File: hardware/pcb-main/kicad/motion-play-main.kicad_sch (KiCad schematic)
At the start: 24 parts, among them J3 LED_Strip, J4 Conn_01x05, J5 Conn_01x05, J6 Conn_01x05, U1 AP2112K-3.3TRG1, U2 T-Display-S3

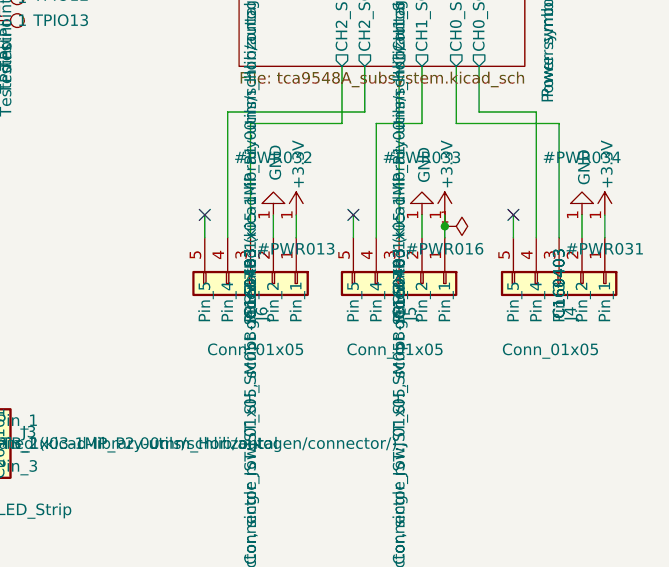
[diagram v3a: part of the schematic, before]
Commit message: JLCPCB pre-flight review: fix 3 LCSC part numbers, add fabrication files
Pre-flight review for JLCPCB fabrication + SMT assembly submission.

LCSC part fixes (data-only, no schematic/PCB design changes):
- J4/J5/J6: C160403 (3-pin JST-SH) → C136657 (5-pin SM05B-SRSS-TB)
- R27: C500724 (0.1Ω 2W, out of stock) → C2903476 (0.1Ω 3W, 94k stock)
- Q2: C3040193 (VBZ3401, 3 units) → C15127 (AO3401A, 1.45M stock, Basic)

Adds fabrication exports (Fabrication Toolkit plugin):
- BOM, CPL/positions, designators, netlist
- DRC and ERC reports
- Pre-flight review report (preflight-review.md)

Remaining advisory: BQ24195RGER (C90862) has only 22 units — order soon.

Made-with: Cursor
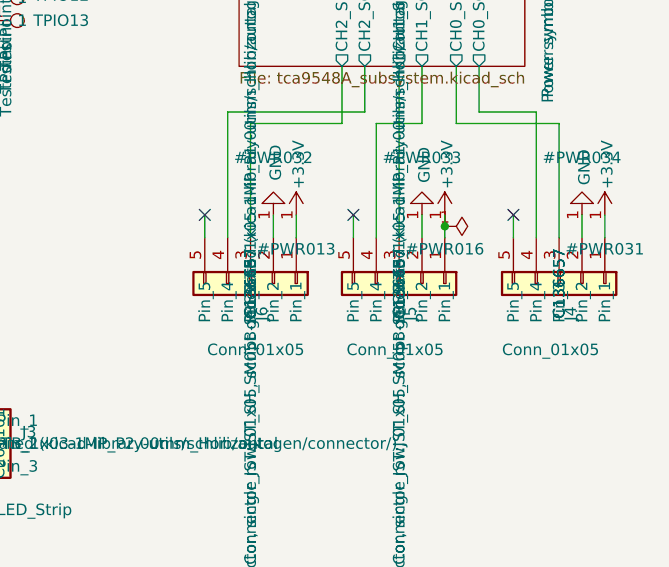
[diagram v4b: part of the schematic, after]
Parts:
- J4, J5, J6: LCSC Part C160403 -> C136657; LCSC Part No C160403 -> C136657
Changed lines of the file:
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@@
 			)
 		)
-		(property "LCSC Part No" "C160403"
+		(property "LCSC Part No" "C136657"
 			(at 205.74 135.89 0)
 			(effects
@@
 			)
 		)
-		(property "LCSC Part" "C160403"
+		(property "LCSC Part" "C136657"
 			(at 205.74 135.89 0)
 			(effects
@@
 			)
 		)
-		(property "LCSC Part No" "C160403"
+		(property "LCSC Part No" "C136657"
 			(at 187.96 135.89 0)
 			(effects
@@
 			)
 		)
-		(property "LCSC Part" "C160403"
+		(property "LCSC Part" "C136657"
 			(at 187.96 135.89 0)
 			(effects
@@
 			)
 		)
-		(property "LCSC Part No" "C160403"
+		(property "LCSC Part No" "C136657"
 			(at 171.45 135.89 0)
 			(effects
@@
 			)
 		)
-		(property "LCSC Part" "C160403"
+		(property "LCSC Part" "C136657"
 			(at 171.45 135.89 0)
 			(effects

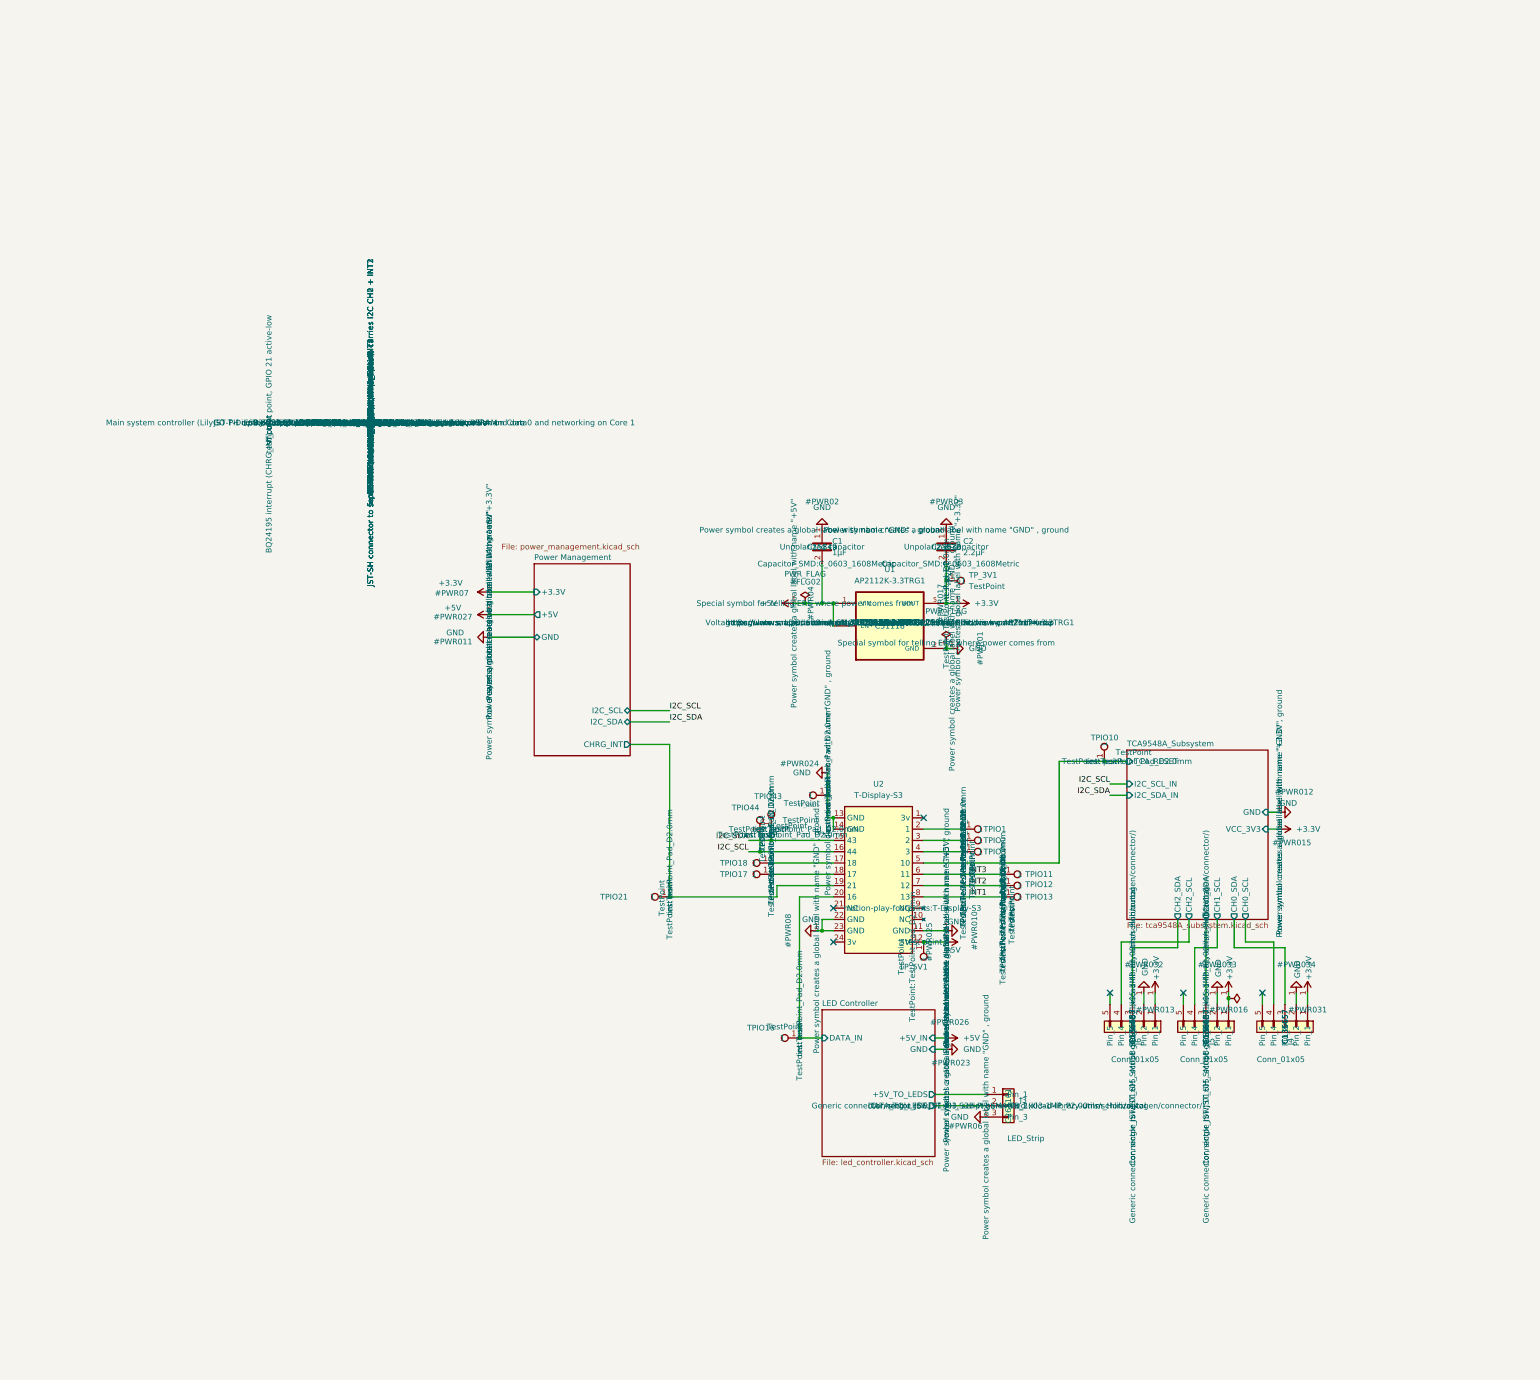
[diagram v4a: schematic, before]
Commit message: Generate ESP32-S3 schematic sheet and apply integration modifications
Phase 1c: created esp32_spec.json and generate_esp32_sheet.py to produce
esp32_s3.kicad_sch with WROOM-1 module, EN/boot circuits, USB series
resistors, decoupling caps, and status LED. All components annotated via
centralized annotate.py.

Phase 1d partial: esp32_integration.py placed AMS1117, USBLC6, power
switch, USB hierarchical labels on power_management sheet; added ESP32
sheet reference and removed U2/U1/unused test points from root sheet.

Fixed modify.py annotate.py path resolution bug. Fixed generator UUID
mismatch that caused kiutils to reset reference designators to '?'.

Made-with: Cursor
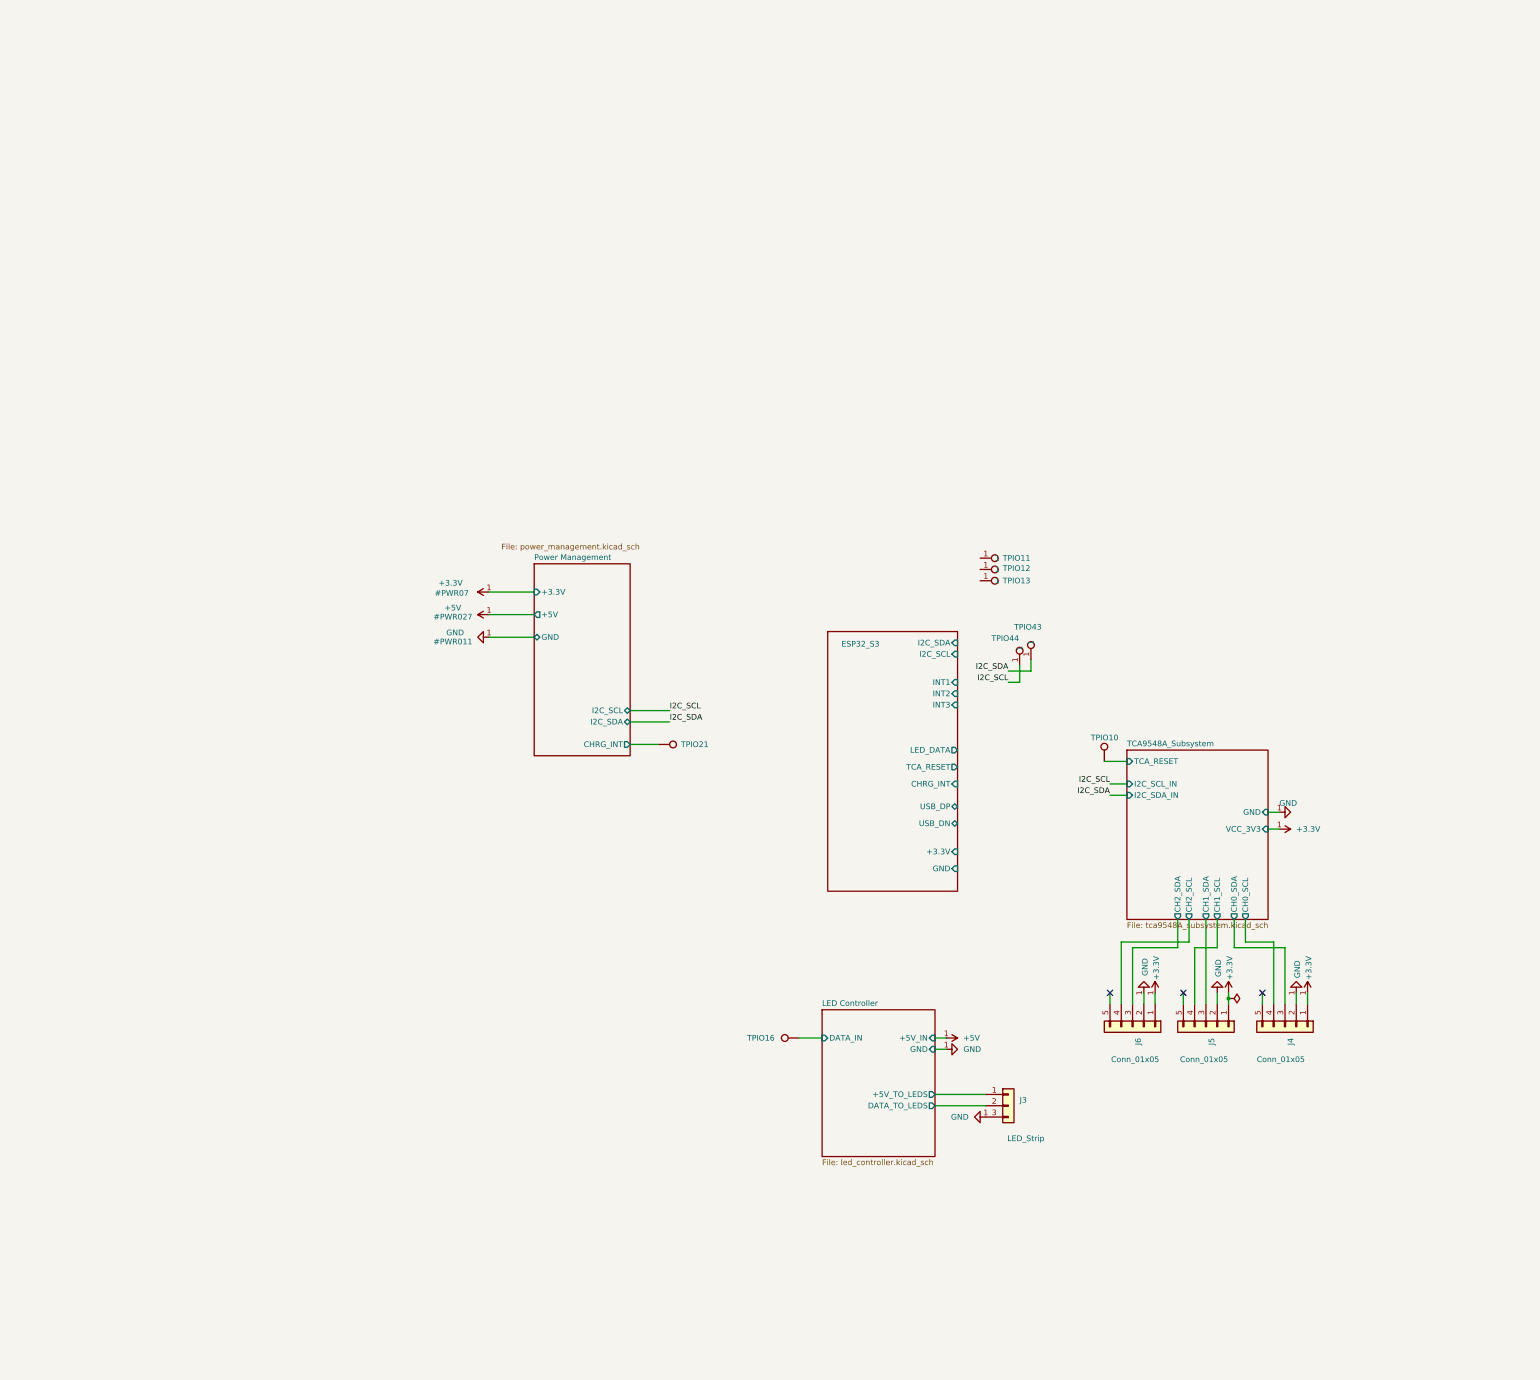
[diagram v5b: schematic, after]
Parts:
- removed C1: 1µF, Capacitor_SMD:C_0603_1608Metric, symbol Device:C
- removed C2: 2.2µF, Capacitor_SMD:C_0603_1608Metric, symbol Device:C
- removed TPIO1, TPIO17, TPIO18, TPIO2, TPIO3, TP_3V1, TP_5V1, TP_GND1: TestPoint, TestPoint:TestPoint_Pad_D2.0mm, symbol Connector:TestPoint
- removed U1: AP2112K-3.3TRG1, motion-play-footprints:SOT95P285X140-5N, symbol motion-play-symbols:AP2112K-3.3TRG1
- removed U2: T-Display-S3, motion-play-footprints:T-Display-S3, symbol motion-play-symbols:T-Display-S3
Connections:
- net INT1: no longer names the net of TPIO13.1
- net INT2: no longer names the net of TPIO12.1
- net INT3: no longer names the net of TPIO11.1
- no-connect marks 6 -> 3
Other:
- added sheet ESP32_S3 (esp32_s3.kicad_sch)
- moved on the sheet: TPIO11, TPIO12, TPIO13, TPIO43, TPIO44

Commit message: Fix Phase 1d schematic issues: SW1, USB pins, +5V, +3.3V direction
- Fix SW1 power switch: pin 3 was wired to VSYS (same as pin 1),
  making the switch always-on. Changed to no-connect so the SPDT
  switch can actually disconnect VSYS from the boost input.
- Add USB_DP/USB_DN sheet pins to power_management reference on root
  so USB data signals can flow between power and root sheets.
- Add +5V hierarchical label to ESP32_S3 sheet and matching sheet pin
  on root, connecting status LED D5 to the global +5V rail.
- Change +3.3V hlabel/pin direction from input to output on power
  management sheet since AMS1117 now produces +3.3V there.
- Add reusable helpers to modify.py: find_sheet_ref, add_pin_to_sheet_ref,
  change_hlabel_shape, change_sheet_pin_direction, label/wire surgery.

Made-with: Cursor
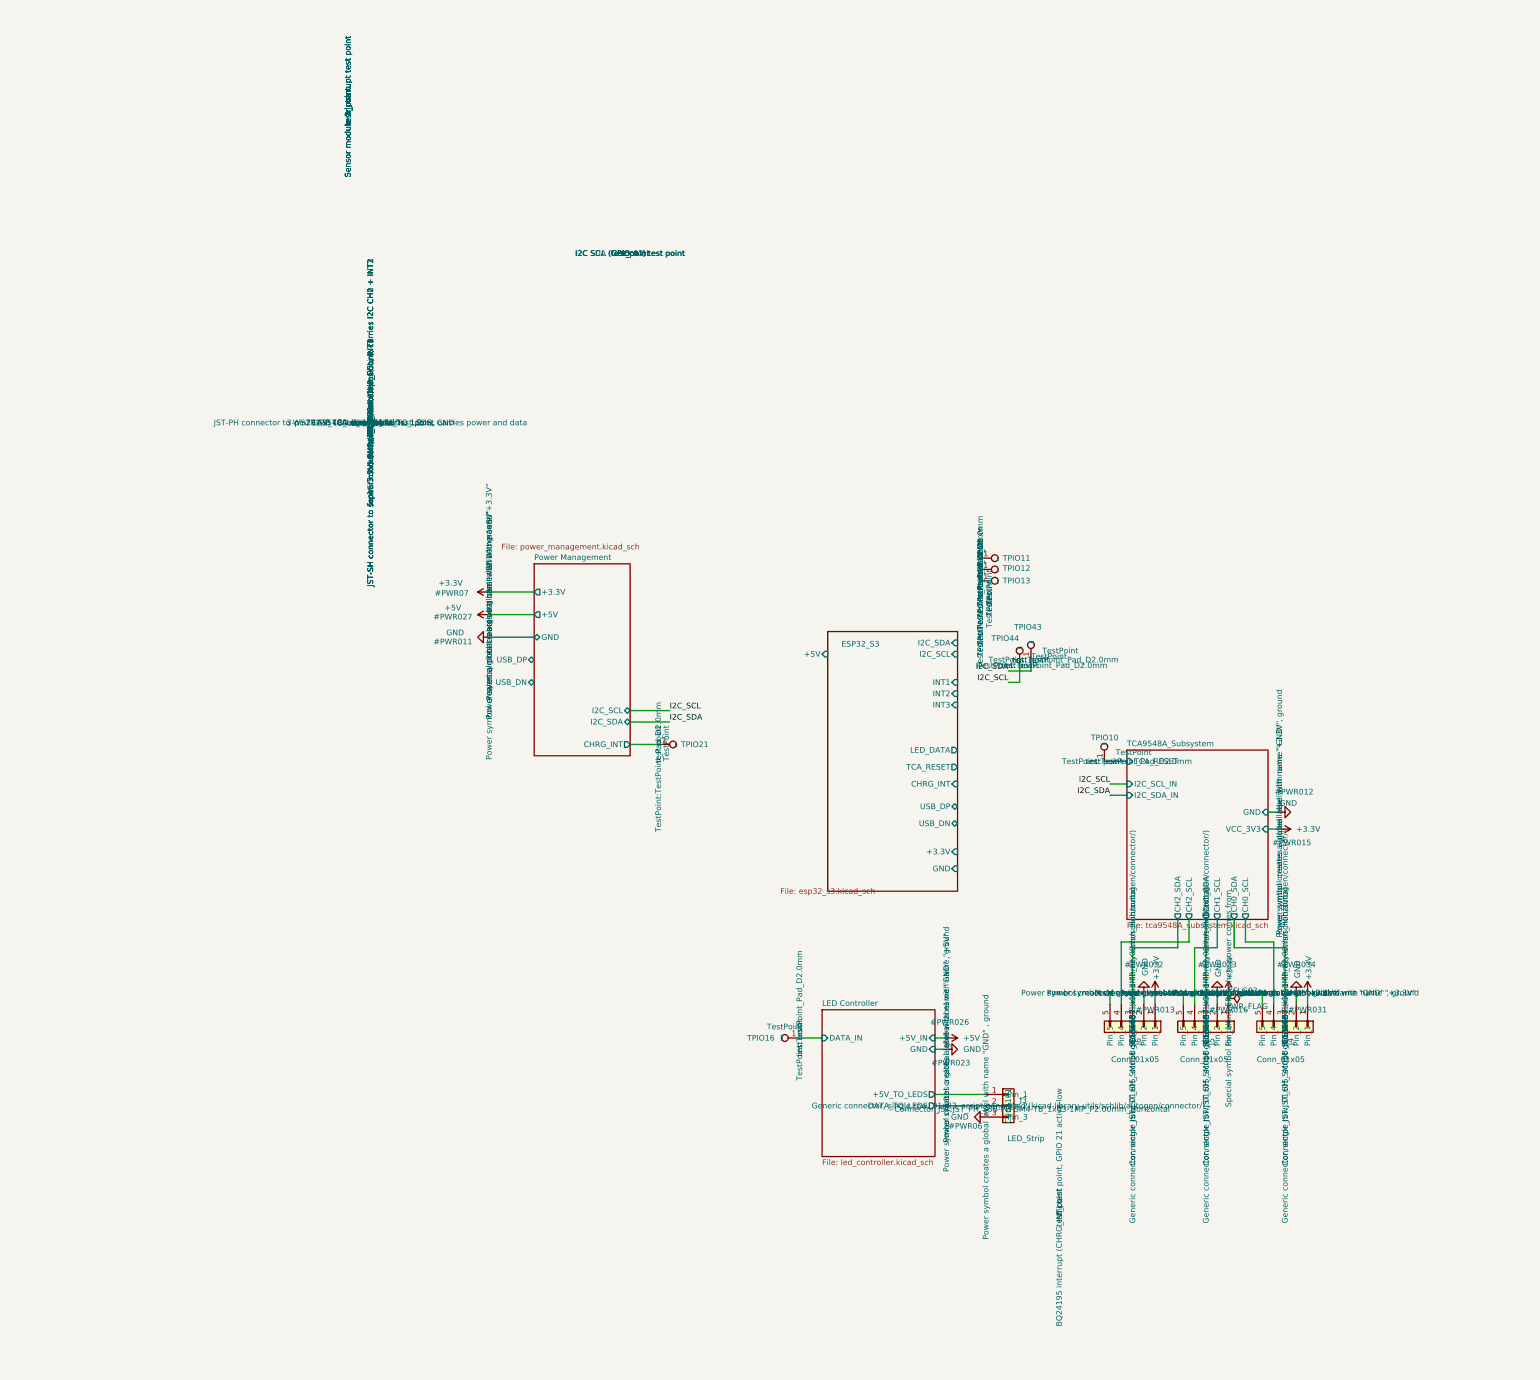
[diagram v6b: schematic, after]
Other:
- sheet ESP32_S3 ports: added +5V; removed none
- sheet Power Management ports: added USB_DN, USB_DP; removed none
